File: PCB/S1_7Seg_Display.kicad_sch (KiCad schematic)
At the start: 6 parts, among them U6 MAX7221xWG, U7 CA56-12EWA, U8 CA56-12EWA

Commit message: Update PCB to seperate ground symbols apporiately. Modify board to sepearte ground path for motor current and all other devices. Add filtering for slide power, hopefully reduce bownout or other issue.
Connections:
- net GND renamed GNDD
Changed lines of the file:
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@@
 	(wire
 		(pts
-			(xy 134.62 86.36) (xy 147.32 86.36)
+			(xy 134.62 86.36) (xy 138.43 86.36)
 		)
 		(stroke
@@
 	(wire
 		(pts
-			(xy 147.32 86.36) (xy 147.32 87.63)
+			(xy 138.43 86.36) (xy 138.43 87.63)
 		)
 		(stroke
@@
 	)
 	(symbol
+		(lib_id "power:GNDD")
+		(at 138.43 87.63 0)
+		(unit 1)
+		(exclude_from_sim no)
+		(in_bom yes)
+		(on_board yes)
+		(dnp no)
+		(fields_autoplaced yes)
+		(property "Reference" "#PWR049"
+			(at 138.43 93.98 0)
+			(effects
+				(font
+					(size 1.27 1.27)
+				)
+				(hide yes)
+			)
+		)
+		(property "Value" "GNDD"
+			(at 138.43 91.44 0)
+			(effects
+				(font
+					(size 1.27 1.27)
+				)
+			)
+		)
+		(property "Footprint" ""
+			(at 138.43 87.63 0)
+			(effects
+				(font
+					(size 1.27 1.27)
+				)
+				(hide yes)
+			)
+		)
+		(property "Datasheet" ""
+			(at 138.43 87.63 0)
+			(effects
+				(font
+					(size 1.27 1.27)
+				)
+				(hide yes)
+			)
+		)
+		(property "Description" "Power symbol creates a global label with name \"GNDD\" , digital ground"
+			(at 138.43 87.63 0)
+			(effects
+				(font
+					(size 1.27 1.27)
+				)
+				(hide yes)
+			)
+		)
+		(pin "1"
+		)
+		(instances
+			(project "UMTK"
+				(path "/2bf3ea67-58b8-47b3-a768-ea6950b40edf/96966801-b9b1-4005-b7bb-fead645709bc"
+					(reference "#PWR049")
+					(unit 1)
+				)
+			)
+		)
+	)
+	(symbol
 		(lib_id "Device:R_US")
 		(at 93.98 87.63 0)
@@
 	)
 	(symbol
-		(lib_id "UMTK-altium-import:GND")
-		(at 147.32 87.63 0)
-		(unit 1)
-		(exclude_from_sim no)
-		(in_bom yes)
-		(on_board yes)
-		(dnp no)
-		(property "Reference" "#PWR064"
-			(at 158.496 88.9 0)
-			(effects
-				(font
-					(size 1.27 1.27)
-				)
-			)
-		)
-		(property "Value" "GND"
-			(at 157.226 91.186 0)
-			(effects
-				(font
-					(size 1.27 1.27)
-				)
-			)
-		)
-		(property "Footprint" ""
-			(at 147.32 87.63 0)
-			(effects
-				(font
-					(size 1.27 1.27)
-				)
-				(hide yes)
-			)
-		)
-		(property "Datasheet" ""
-			(at 147.32 87.63 0)
-			(effects
-				(font
-					(size 1.27 1.27)
-				)
-				(hide yes)
-			)
-		)
-		(property "Description" "Power symbol creates a global label with name 'GND'"
-			(at 147.32 87.63 0)
-			(effects
-				(font
-					(size 1.27 1.27)
-				)
-				(hide yes)
-			)
-		)
-		(pin ""
-		)
-		(instances
-			(project "UMTK"
-				(path "/2bf3ea67-58b8-47b3-a768-ea6950b40edf/96966801-b9b1-4005-b7bb-fead645709bc"
-					(reference "#PWR064")
-					(unit 1)
-				)
-			)
-		)
-	)
-	(symbol
 		(lib_id "Driver_LED:MAX7221xWG")
 		(at 109.22 115.57 0)
@@
 	)
 	(symbol
-		(lib_id "UMTK-altium-import:GND")
+		(lib_id "power:GNDD")
 		(at 109.22 144.78 0)
 		(unit 1)
@@
 		(on_board yes)
 		(dnp no)
-		(property "Reference" "#PWR049"
-			(at 120.396 146.05 0)
-			(effects
-				(font
-					(size 1.27 1.27)
-				)
-			)
-		)
-		(property "Value" "GND"
-			(at 119.126 148.336 0)
+		(fields_autoplaced yes)
+		(property "Reference" "#PWR047"
+			(at 109.22 151.13 0)
+			(effects
+				(font
+					(size 1.27 1.27)
+				)
+				(hide yes)
+			)
+		)
+		(property "Value" "GNDD"
+			(at 109.22 148.59 0)
 			(effects
 				(font
@@
 			)
 		)
-		(property "Description" "Power symbol creates a global label with name 'GND'"
+		(property "Description" "Power symbol creates a global label with name \"GNDD\" , digital ground"
 			(at 109.22 144.78 0)
 			(effects
@@
 			)
 		)
-		(pin ""
+		(pin "1"
 		)
 		(instances
 			(project "UMTK"
 				(path "/2bf3ea67-58b8-47b3-a768-ea6950b40edf/96966801-b9b1-4005-b7bb-fead645709bc"
-					(reference "#PWR049")
+					(reference "#PWR047")
 					(unit 1)
 				)

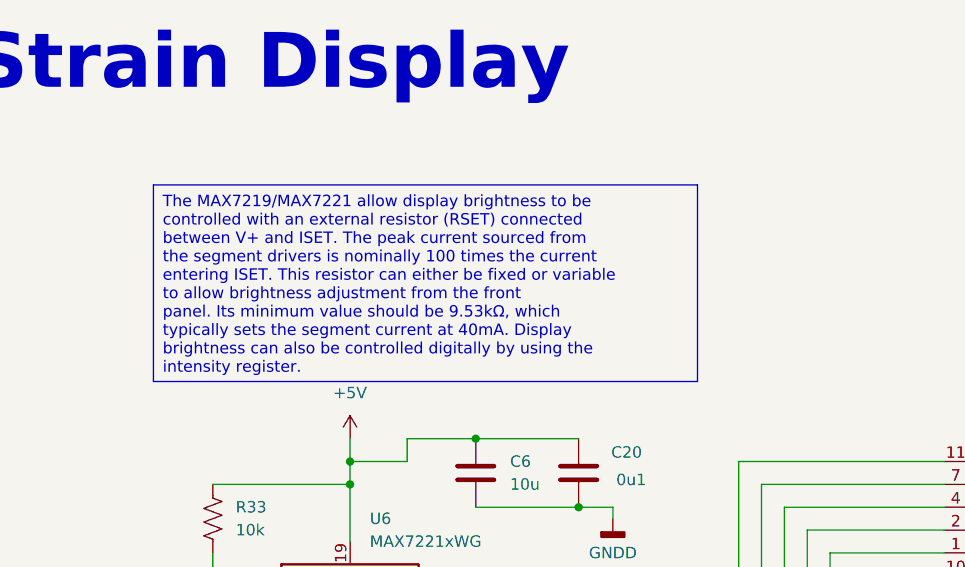
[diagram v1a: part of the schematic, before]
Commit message: WIP Adding adudino onboard, so far copying pro mega
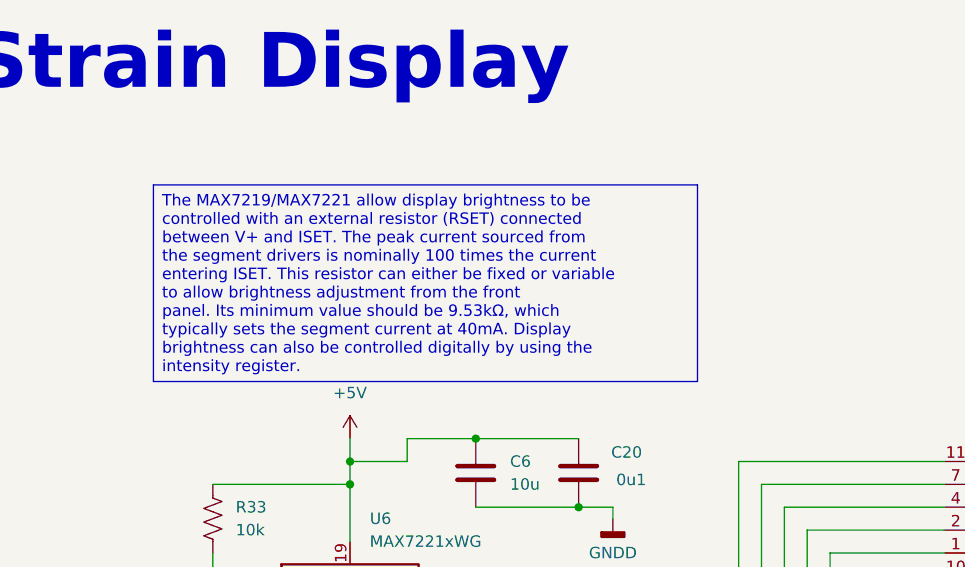
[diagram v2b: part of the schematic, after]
